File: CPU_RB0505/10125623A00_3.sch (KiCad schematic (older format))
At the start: 45 parts, among them IC10 DS1305E, IC11 OP295, IC12 MAX690ACSA, IC31 M41T94MQ6E, Q3 32,768KHz, Q5 32,768KHz, T14 2N7002, T20 BS170F, T21 2N7002, T3 BSS84

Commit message: Schematic symbols updated with BOM fields
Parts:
- BUZ1: Description (none) -> BUZZER, 12V, 30MA, 85DB; Item Number (none) -> 10023244; Manufacturer (none) -> STAR MICRONICS INC.; Manufacturer_Desc (none) -> MAGNETIC BUZZER; Manufacturer_No (none) -> HMB-12
- C39, C43, C45, C50, C53: Description (none) -> CAPACITOR CERAMIC,10NF,+/-10%,50V,0603; Item Number (none) -> 10022508; Manufacturer (none) -> YAGEO_RMS1; Manufacturer2 (none) -> YAGEO_RMS1; Manufacturer3 (none) -> KEMET_RMS1; Manufacturer4 (none) -> YAGEO_RMS1; Manufacturer_Desc (none) -> CAPACITOR, CERAMIC, MULTILAYER, 50 V, X7R, 0.01 UF, SURFACE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; Manufacturer_Desc2 (none) -> CAPACITOR, CERAMIC, MULTILAYER, 50 V, X7R, 0.01 UF, SURFACE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; Manufacturer_Desc3 (none) -> CERAMIC CHIP CAPACITOR; Manufacturer_Desc4 (none) -> CAPACITOR, CERAMIC, MULTILAYER, 50 V, X7R, 0.01 UF, SURFACE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; Manufacturer_No (none) -> 223858615636; Manufacturer_No2 (none) -> 223858615536; Manufacturer_No3 (none) -> C0603C103K5RACTU; Manufacturer_No4 (none) -> CC0603KRX7R9BB103
- C42, C44, C49, C77, C78: Description (none) -> CAPACITOR,100NF,16V,+/-10%,X7R,0402; Item Number (none) -> 10022607; Manufacturer (none) -> MURATA; Manufacturer2 (none) -> YAGEO_RMS1; Manufacturer3 (none) -> YAGEO_RMS1; Manufacturer4 (none) -> MURATA MANUFACTURING CO., LTD.; Manufacturer_Desc (none) -> CAPACITOR, CERAMIC, MULTILAYER, 16V, X7R, 0.1UF, 0402; Manufacturer_Desc2 (none) -> CAP CER 0.1uF 16V X7R 10% 0402; Manufacturer_Desc3 (none) -> CAPACITOR, CERAMIC, MULTILAYER, 16 V, X7R, 0.1 UF, SURFACE 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; Manufacturer_Desc4 (none) -> MONOLITHIC CERAMIC CAPACITOR; Manufacturer_No (none) -> GRM155R71C104JA88J; Manufacturer_No2 (none) -> CC0402KRX7R7BB104; Manufacturer_No3 (none) -> 223878715649; Manufacturer_No4 (none) -> GRM155R71C104KA88D
- C54: Description (none) -> CAPACITOR CERAMIC,1UF,16V,+/-10%, 0805; Item Number (none) -> 10022967; Manufacturer (none) -> KEMET_RMS1; Manufacturer2 (none) -> KEMET_RMS1; Manufacturer3 (none) -> YAGEO_RMS1; Manufacturer4 (none) -> MURATA_RMS1; Manufacturer_Desc (none) -> CERAMIC CHIP CAPACITOR; Manufacturer_Desc2 (none) -> CERAMIC SURFACE MOUNT; Manufacturer_Desc3 (none) -> CAPACITOR, CERAMIC, MULTILAYER, 16 V, Y5V, 1 UF, SURFACE MO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; Manufacturer_Desc4 (none) -> MONOLITHIC CERAMIC CAPACITOR; Manufacturer_No (none) -> C0805C105Z4VACTU; Manufacturer_No2 (none) -> C0805C105Z4VAC; Manufacturer_No3 (none) -> CC0805ZRY5V7BB105; Manufacturer_No4 (none) -> GRM216B31C105KA87D
- C84: Description (none) -> CAPACITOR CERAMIC, 1NF,50V,+/-10%, 0402; Item Number (none) -> 10022971; Manufacturer (none) -> YAGEO_RMS1; Manufacturer2 (none) -> YAGEO_RMS1; Manufacturer3 (none) -> KEMET_RMS1; Manufacturer4 (none) -> YAGEO_RMS1; Manufacturer_Desc (none) -> CAPACITOR, CERAMIC, MULTILAYER, 50 V, X7R, 0.001 UF, SURFAC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; Manufacturer_Desc2 (none) -> CAPACITOR, CERAMIC, MULTILAYER, 50 V, X7R, 0.001 UF, SURFAC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; Manufacturer_Desc3 (none) -> CAP, CER, 0.001UF, 50V, 10%, X7R, 0402; Manufacturer_Desc4 (none) -> CAPACITOR, CERAMIC, MULTILAYER, 50 V, X7R, 0.001 UF, SURFAC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; Manufacturer_No (none) -> CC0402KRX7R9BB102*; Manufacturer_No2 (none) -> 223858715623; Manufacturer_No3 (none) -> C0402C102K5RACTU; Manufacturer_No4 (none) -> 223858715523
- D12: Description (none) -> DIODE ZENER, 500MW, 12V, SOD-80C; Item Number (none) -> 10020994; Manufacturer (none) -> NXP SEMICONDUCTORS_RMS1; Manufacturer2 (none) -> NXP SEMICONDUCTORS_RMS1; Manufacturer_Desc2 (none) -> VOLTAGE REGULATOR DIODE; Manufacturer_No (none) -> BZV55-C12,115; Manufacturer_No2 (none) -> BZV55-C12
- D14: Description (none) -> DIODE SCHOTTKY DOUBLE,30V, 200MA,SOT23; Item Number (none) -> 10022653; Manufacturer (none) -> NXP SEMICONDUCTORS_RMS1; Manufacturer2 (none) -> NXP SEMICONDUCTORS_RMS1; Manufacturer_Desc2 (none) -> SCHOTTKY BARRIER DOUBLE DIODE; Manufacturer_No (none) -> BAT54C,215; Manufacturer_No2 (none) -> BAT54C
- D15, D16: Description (none) -> DIODE SCHOTTKY, 40V, 1A; Item Number (none) -> 10097253; Manufacturer (none) -> DIODES INC_RMS1; Manufacturer_Desc (none) -> SURFACE MOUNT SCHOTTKY BARRIER RECTIFIER; Manufacturer_No (none) -> 1N5819HW-7-F
- G1: Description (none) -> LITHIUM, 3V, 35MAH; Item Number (none) -> 10022884; Manufacturer (none) -> SONY_RMS1; Manufacturer2 (none) -> MAXELL; Manufacturer3 (none) -> VARTA (917650); Manufacturer_Desc (none) -> COIN CELL BATTERY; Manufacturer_Desc3 (none) -> BATTERY; Manufacturer_No (none) -> CR1220-B1A; Manufacturer_No2 (none) -> CR1220; Manufacturer_No3 (none) -> CR 1220
- IC10: Description (none) -> IC,REALTIMECLOCK, TSSOP; Item Number (none) -> 10022965; Manufacturer (none) -> MAXIM_RMS1; Manufacturer2 (none) -> MAXIM_RMS1; Manufacturer_No (none) -> DS1305E+; Manufacturer_No2 (none) -> DS1305E+T&R
- IC11: Description (none) -> DOUBLE AMPLIFIER RAIL TO RAIL, SO8; Item Number (none) -> 10022969; Manufacturer (none) -> ANALOG DEVICES, INC.; Manufacturer2 (none) -> ANALOG DEVICES, INC.; Manufacturer_Desc (none) -> IC OPAMP GP R-R 85KHZ DUAL 8SOIC; Manufacturer_Desc2 (none) -> IC OPAMP DUAL RAIL-RAIL 8SOIC; Manufacturer_No (none) -> OP295GSZ-REEL7; Manufacturer_No2 (none) -> OP295GSZ
- IC12: Description (none) -> IC,MICROPROCESSOR SUPERVISOR CIRCUIT,SO8; Item Number (none) -> 10022970; Manufacturer (none) -> MAXIM_RMS1; Manufacturer2 (none) -> MAXIM_RMS1; Manufacturer_Desc2 (none) -> MICROPROCESSOR SUPERVISORY CIRCUIT; Manufacturer_No (none) -> MAX690ACSA+T; Manufacturer_No2 (none) -> MAX690ACSA+
- Q5: Description (none) -> CRYSTAL QUARTZ 32.768KHZ; Item Number (none) -> 10023250; Manufacturer (none) -> IQD; Manufacturer_Desc (none) -> CRYSTAL QUARTZ 32.768KHZ; Manufacturer_No (none) -> LFXTAL003000REEL
- R17: Description (none) -> RESISTOR, 15K OHM, 0603, +/-1%; Item Number (none) -> 10023238; Manufacturer (none) -> ASJ; Manufacturer2 (none) -> VISHAY_RMS1; Manufacturer3 (none) -> YAGEO_RMS1; Manufacturer4 (none) -> YAGEO_RMS1; Manufacturer5 (none) -> YAGEO_RMS1; Manufacturer_Desc2 (none) -> THICK FILM RECTANGULAR CHIP RESISTOR; Manufacturer_Desc3 (none) -> RESISTOR, METAL GLAZE/THICK FILM, 0.1 W, 1 %, 100 PPM, 1500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; Manufacturer_Desc4 (none) -> RESISTOR, METAL GLAZE/THICK FILM, 0.1 W, 1 %, 100 PPM, 1500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; Manufacturer_Desc5 (none) -> RESISTOR, METAL GLAZE/THICK FILM, 0.1 W, 1 %, 100 PPM, 1500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; Manufacturer_No (none) -> CR16153FL; Manufacturer_No2 (none) -> CRCW060315K0FKEA; Manufacturer_No3 (none) -> 232270461503L; Manufacturer_No4 (none) -> RC0603FR-0715KL; Manufacturer_No5 (none) -> 232270461503
- R18: Description (none) -> RESISTOR,1.5K OHM,0.063W,+/-1%,0603; Item Number (none) -> 10022700; Manufacturer (none) -> YAGEO_RMS1; Manufacturer2 (none) -> YAGEO_RMS1; Manufacturer3 (none) -> KOA SPEER; Manufacturer4 (none) -> YAGEO_RMS1; Manufacturer_Desc (none) -> RESISTOR, METAL GLAZE/THICK FILM, 0.1 W, 1 %, 100 PPM, 1500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; Manufacturer_Desc2 (none) -> RESISTOR, METAL GLAZE/THICK FILM, 0.1 W, 1 %, 100 PPM, 1500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; Manufacturer_Desc3 (none) -> THICK FILM CHIP RESISTOR; Manufacturer_Desc4 (none) -> RESISTOR, METAL GLAZE/THICK FILM, 0.1 W, 1 %, 100 PPM, 1500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; Manufacturer_No (none) -> 232270461502; Manufacturer_No2 (none) -> 232270461502L; Manufacturer_No3 (none) -> RK73H1JTTD1501F; Manufacturer_No4 (none) -> RC0603FR-071K5L
- R19: Description (none) -> RESISTOR, 75K OHM, 0603, +/-1%; Item Number (none) -> 10023239; Manufacturer (none) -> MULTICOMP (920630); Manufacturer_Desc (none) -> THICK FILM CHIP RESISTOR; Manufacturer_No (none) -> MC 0.063W 0603 1% 75K
- R28, R29, R53, R54: Description (none) -> RESISTOR,10K OHM, 0.063W,+/-5%,0603; Item Number (none) -> 10097266; Manufacturer (none) -> YAGEO_RMS1; Manufacturer2 (none) -> YAGEO_RMS1; Manufacturer3 (none) -> VISHAY_RMS1; Manufacturer4 (none) -> ASJ; Manufacturer5 (none) -> YAGEO_RMS1; Manufacturer_Desc (none) -> RESISTOR, METAL GLAZE/THICK FILM, 0.1 W, 5 %, 100 PPM, 1000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; Manufacturer_Desc2 (none) -> RESISTOR, METAL GLAZE/THICK FILM, 0.1 W, 5 %, 100 PPM, 1000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; Manufacturer_Desc3 (none) -> THICK FILM RECTANGULAR CHIP RESISTOR; Manufacturer_Desc4 (none) -> THICK FILM CHIP RESISTOR; Manufacturer_Desc5 (none) -> RESISTOR, METAL GLAZE/THICK FILM, 0.1 W, 5 %, 100 PPM, 1000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; Manufacturer_No (none) -> 232270260103L; Manufacturer_No2 (none) -> 232270260103; Manufacturer_No3 (none) -> CRCW060310K0JNEA; Manufacturer_No4 (none) -> CR16-103JL; Manufacturer_No5 (none) -> RC0603JR-0710KL
- R52: Description (none) -> RESISTOR 10 OHM, 0.125W, +/-5%,0805; Item Number (none) -> 10023242; Manufacturer (none) -> YAGEO_RMS1; Manufacturer2 (none) -> KOA SPEER; Manufacturer3 (none) -> YAGEO_RMS1; Manufacturer4 (none) -> YAGEO_RMS1; Manufacturer_Desc (none) -> RESISTOR, METAL GLAZE/THICK FILM, 0.125 W, 5 %, 200 PPM, 10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; Manufacturer_Desc2 (none) -> THICK FILM CHIP RESISTOR; Manufacturer_Desc3 (none) -> RESISTOR, METAL GLAZE/THICK FILM, 0.125 W, 5 %, 200 PPM, 10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; Manufacturer_Desc4 (none) -> RESISTOR, METAL GLAZE/THICK FILM, 0.125 W, 5 %, 200 PPM, 10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; Manufacturer_No (none) -> RC0805JR-0710RL; Manufacturer_No2 (none) -> RK73B2ATTD100J; Manufacturer_No3 (none) -> 232273061109L; Manufacturer_No4 (none) -> 232273061109
- R55, R56, R59, R65, R8, R9: Description (none) -> RESISTOR,100 K OHM, 0.063W +/-5%; Item Number (none) -> 10022732; Manufacturer (none) -> YAGEO_RMS1; Manufacturer2 (none) -> YAGEO_RMS1; Manufacturer3 (none) -> YAGEO_RMS1; Manufacturer4 (none) -> PANASONIC_RMS1; Manufacturer_Desc (none) -> RESISTOR, METAL GLAZE/THICK FILM, 0.1 W, 5 %, 100 PPM, 1000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; Manufacturer_Desc2 (none) -> RESISTOR, METAL GLAZE/THICK FILM, 0.1 W, 5 %, 100 PPM, 1000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; Manufacturer_Desc3 (none) -> RESISTOR, METAL GLAZE/THICK FILM, 0.1 W, 5 %, 100 PPM, 1000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; Manufacturer_Desc4 (none) -> THICK FILM CHIP RESISTOR; Manufacturer_No (none) -> 232270260104L; Manufacturer_No2 (none) -> 232270260104; Manufacturer_No3 (none) -> RC0603JR-07100KL; Manufacturer_No4 (none) -> ERJ3GEYJ104V
- R57: Description (none) -> RESISTOR,1.37K OHM,0.063W,+/-0.1%,0603; Item Number (none) -> 10097270; Manufacturer (none) -> SUSUMU CO.; Manufacturer2 (none) -> TYCO ELECTRONICS; Manufacturer3 (none) -> TYCO ELECTRONICS; Manufacturer4 (none) -> VISHAY_RMS1; Manufacturer5 (none) -> WELWYN; Manufacturer_Desc2 (none) -> THIN FILM PRECISION CHIP RESISTOR; Manufacturer_Desc3 (none) -> THIN FILM PRECISION CHIP RESISTOR; Manufacturer_Desc4 (none) -> PRECISION CHIP RESISTOR; Manufacturer_Desc5 (none) -> PRECISION SURFACE MOUNT RESISTOR; Manufacturer_No (none) -> RG1608P-1371-B-T5; Manufacturer_No2 (none) -> 3-1879219-4; Manufacturer_No3 (none) -> CPF0603B-1K37E; Manufacturer_No4 (none) -> TNPW06031K37BEEA; Manufacturer_No5 (none) -> PCF0603R-1K37BI
- R58: Description (none) -> RESISTOR, 100K OHM, 0.063W,+/-0.1%,0603; Item Number (none) -> 10097271; Manufacturer (none) -> SUSUMU CO.; Manufacturer2 (none) -> WELWYN; Manufacturer3 (none) -> YAGEO_RMS1; Manufacturer_Desc (none) -> RES SMD 100K OHM 0.1% 1/10W 0603; Manufacturer_Desc2 (none) -> LOW VALUE FLAT CHIP RESISTOR; Manufacturer_Desc3 (none) -> RESISTOR, THIN FILM, 0.1 W, 0.1 %, 25 PPM, 100000 OHM, SURF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; Manufacturer_No (none) -> RG1608P-104-B-T5; Manufacturer_No2 (none) -> PCF0603R-100KBI; Manufacturer_No3 (none) -> RT0603BRD07100KL
- T14, T21: Description (none) -> TRANSISTOR MOSFET N CHANNEL 60V, 0.18A; Item Number (none) -> 10097274; Manufacturer (none) -> ON SEMICONDUCTOR_RMS1; Manufacturer2 (none) -> NXP SEMICONDUCTORS_RMS1; Manufacturer3 (none) -> NXP SEMICONDUCTORS_RMS1; Manufacturer_Desc (none) -> SMALL SIGNAL MOSFET; Manufacturer_Desc3 (none) -> N-CHANNEL TRENCHMOS FET; Manufacturer_No (none) -> 2N7002LT1G; Manufacturer_No2 (none) -> 2N7002,215; Manufacturer_No3 (none) -> 2N7002
- T20: Description (none) -> TRANSISTOR, MOSFET, N-CHANNEL, 60V, 0.5A.SOT23; Item Number (none) -> 10022956; Manufacturer (none) -> FAIRCHILD SEMICONDUCTOR_RMS1; Manufacturer2 (none) -> DIODES INC_RMS1; Manufacturer_Desc (none) -> MOSFET N-CH 60V 500MA SOT-23; Manufacturer_Desc2 (none) -> N-CHANNEL MOSFET; Manufacturer_No (none) -> MMBF170; Manufacturer_No2 (none) -> MMBF170-7-F
- T3: Description (none) -> TRANSISTOR, P CHANNEL, 50V, 0.13A, 5 OHM, SOT23; Item Number (none) -> 10022157; Manufacturer (none) -> NXP SEMICONDUCTORS_RMS1; Manufacturer2 (none) -> ON SEMICONDUCTOR_RMS1; Manufacturer3 (none) -> NXP SEMICONDUCTORS_RMS1; Manufacturer_Desc (none) -> MOSFET P CHANNEL; Manufacturer_Desc2 (none) -> POWER MOSFET; Manufacturer_No (none) -> BSS84; Manufacturer_No2 (none) -> BSS84LT1G; Manufacturer_No3 (none) -> BSS84,215
- V2: Description (none) -> 3 WAY, PROPORTIONAL VALVE; Item Number (none) -> 10025112; Manufacturer (none) -> FAS; Manufacturer_Desc (none) -> 3 WAY PROPORTIONAL VALVE; Manufacturer_No (none) -> S142.0048A

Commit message: back anotate from cmp file
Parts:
- BUZ1: footprint 10125623A00:F_HMB -> AllModules:HMB12_1
- C39, C43, C45, C50, C53: footprint 10125623A00:C0805 -> AllModules:C0603_1
- C42, C44, C49, C77, C78, C84: footprint 10125623A00:C0805 -> AllModules:C0402_1
- C54: footprint 10125623A00:C0805 -> AllModules:C0805_1
- D12: footprint 10125623A00:SOT23DIO -> AllModules:SOD80_1
- D14: footprint 10125623A00:SOT23_DI -> AllModules:SOT23-1G_1
- D15, D16: footprint 10125623A00:SOD87 -> AllModules:SOD87_1
- G1: footprint 10125623A00:KEY_3000 -> AllModules:CR1220-3000_1
- IC10: footprint 10125623A00:TSSOP20 -> AllModules:TSSOP20_SANS-MIRE_1
- IC11: footprint 10125623A00:SO8 -> AllModules:MX.A8_COMPOSANT_1
- IC12: footprint 10125623A00:SO08 -> AllModules:MX.A8_COMPOSANT_1
- IC31: footprint 10125623A00:SO16 -> AllModules:MX.A16_COMPOSANT_1
- Q3, Q5: footprint 10125623A00:86SMX -> AllModules:85SMX_1
- R17, R18, R19, R28, R29, R53, R54, R55, R56, R57, R58, R59, R65, R8, R9: footprint 10125623A00:R0805 -> AllModules:R0603_1
- R52: footprint 10125623A00:R0805 -> AllModules:R0805_1
- T14, T20, T21: footprint 10125623A00:DPAK -> AllModules:SOT23-GSD_1
- T3: footprint 10125623A00:SOT23MOS -> AllModules:SOT23-GSD_1
- V2: footprint 10125623A00:FAS-PPS-1P-3NIP-INJ -> AllModules:S142.0011-SANS-FIX_1

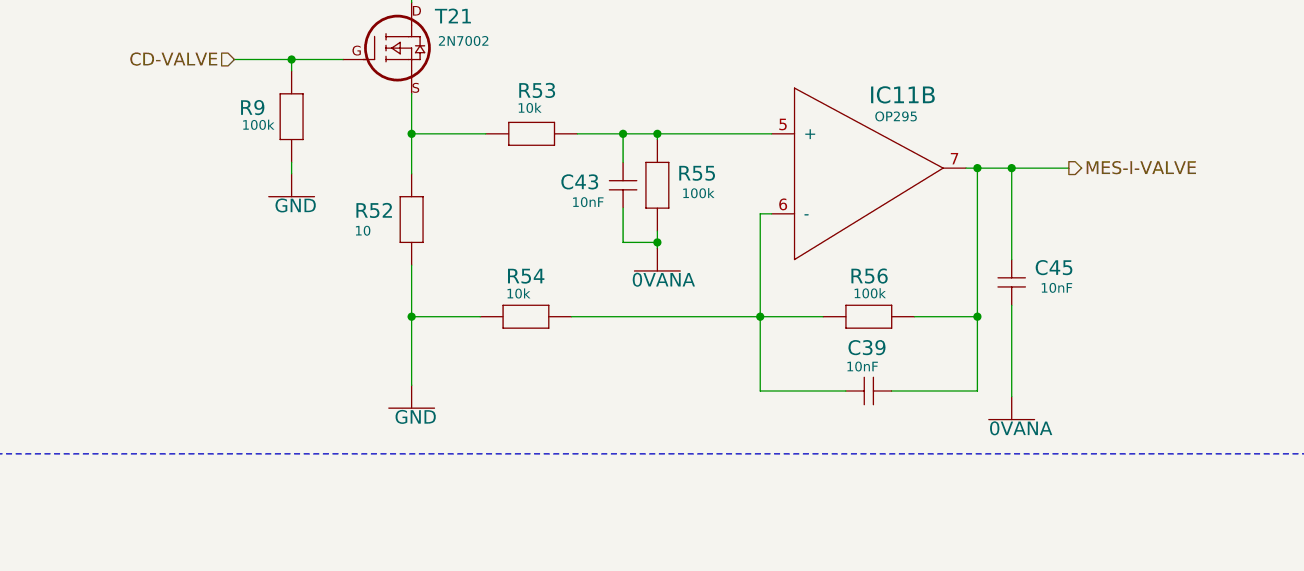
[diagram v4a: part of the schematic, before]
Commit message: fix erc errors, change many pin electrical types
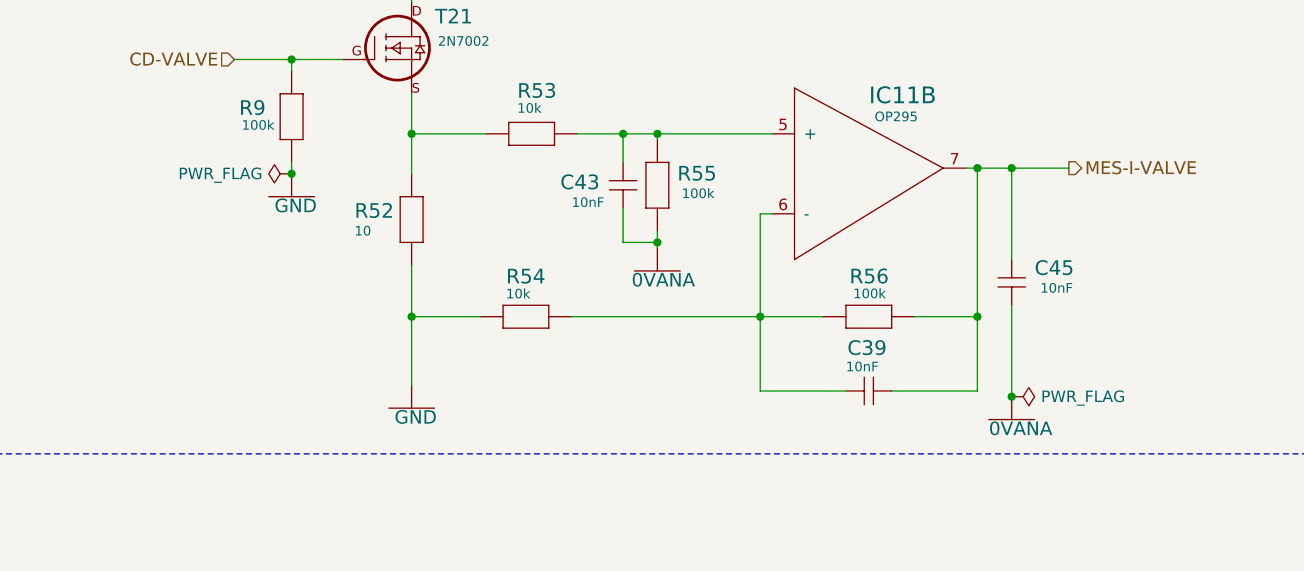
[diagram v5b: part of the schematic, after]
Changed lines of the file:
@@
-$EndComp
-$Comp
-L cpu-board:LM358 IC11
-U 3 1 D9B46218
-P 7325 2700
-AR Path="/D9B46218" Ref="IC11"  Part="3"
-AR Path="/5E924756/D9B46218" Ref="IC11"  Part="3"
-F 0 "IC11" H 7525 2950 73  0001 L BNN
-F 1 "OP295" H 7675 2850 73  0001 L BNN
-F 2 "AllModules:MX.A8_COMPOSANT_1" H 7325 2700 50  0001 C CNN
-F 3 "" H 7325 2700 50  0001 C CNN
-F 4 "DOUBLE AMPLIFIER RAIL TO RAIL, SO8" H 7325 2700 50  0001 C CNN "Description"
-F 5 "10022969" H 7325 2700 50  0001 C CNN "Item Number"
-F 6 "ANALOG DEVICES, INC." H 7325 2700 50  0001 C CNN "Manufacturer"
-F 7 "OP295GSZ-REEL7" H 7325 2700 50  0001 C CNN "Manufacturer_No"
-F 8 "IC OPAMP GP R-R 85KHZ DUAL 8SOIC" H 7325 2700 50  0001 C CNN "Manufacturer_Desc"
-F 9 "ANALOG DEVICES, INC." H 7325 2700 50  0001 C CNN "Manufacturer2"
-F 10 "OP295GSZ" H 7325 2700 50  0001 C CNN "Manufacturer_No2"
-F 11 "IC OPAMP DUAL RAIL-RAIL 8SOIC" H 7325 2700 50  0001 C CNN "Manufacturer_Desc2"
-	3    7325 2700
-	1    0    0    -1
 $EndComp
 $Comp
@@
 NoConn ~ 3225 2850
 NoConn ~ 2125 3350
-$Comp
-L cpu-board:LM358 IC11
-U 1 1 D9B46210
-P 7375 2700
-AR Path="/D9B46210" Ref="IC11"  Part="1"
-AR Path="/5E924756/D9B46210" Ref="IC11"  Part="1"
-F 0 "IC11" H 7425 2950 64  0000 L BNN
-F 1 "OP295" H 7450 2863 42  0000 L BNN
-F 2 "AllModules:MX.A8_COMPOSANT_1" H 7375 2700 50  0001 C CNN
-F 3 "" H 7375 2700 50  0001 C CNN
-F 4 "DOUBLE AMPLIFIER RAIL TO RAIL, SO8" H 7325 2700 50  0001 C CNN "Description"
-F 5 "10022969" H 7325 2700 50  0001 C CNN "Item Number"
-F 6 "ANALOG DEVICES, INC." H 7325 2700 50  0001 C CNN "Manufacturer"
-F 7 "OP295GSZ-REEL7" H 7325 2700 50  0001 C CNN "Manufacturer_No"
-F 8 "IC OPAMP GP R-R 85KHZ DUAL 8SOIC" H 7325 2700 50  0001 C CNN "Manufacturer_Desc"
-F 9 "ANALOG DEVICES, INC." H 7325 2700 50  0001 C CNN "Manufacturer2"
-F 10 "OP295GSZ" H 7325 2700 50  0001 C CNN "Manufacturer_No2"
-F 11 "IC OPAMP DUAL RAIL-RAIL 8SOIC" H 7325 2700 50  0001 C CNN "Manufacturer_Desc2"
-	1    7375 2700
-	1    0    0    -1
-$EndComp
 Wire Wire Line
 	3850 3025 3850 3100
@@
 	3225 4925 3825 4925
 NoConn ~ 3525 5075
+$Comp
+L power:PWR_FLAG #FLG0104
+U 1 1 5ED7B35B
+P 11375 6300
+F 0 "#FLG0104" H 11375 6375 50  0001 C CNN
+F 1 "PWR_FLAG" V 11375 6427 50  0000 L CNN
+F 2 "" H 11375 6300 50  0001 C CNN
+F 3 "~" H 11375 6300 50  0001 C CNN
+	1    11375 6300
+	0    -1   -1   0
+$EndComp
+Connection ~ 11375 6300
+$Comp
+L power:PWR_FLAG #FLG0105
+U 1 1 5ED7BF1F
+P 14525 7275
+F 0 "#FLG0105" H 14525 7350 50  0001 C CNN
+F 1 "PWR_FLAG" V 14525 7403 50  0000 L CNN
+F 2 "" H 14525 7275 50  0001 C CNN
+F 3 "~" H 14525 7275 50  0001 C CNN
+	1    14525 7275
+	0    1    1    0
+$EndComp
+Connection ~ 14525 7275
+$Comp
+L cpu-board:LM358 IC11
+U 1 1 D9B46210
+P 7375 2700
+AR Path="/D9B46210" Ref="IC11"  Part="1"
+AR Path="/5E924756/D9B46210" Ref="IC11"  Part="1"
+F 0 "IC11" H 7425 2950 64  0000 L BNN
+F 1 "OP295" H 7450 2863 42  0000 L BNN
+F 2 "AllModules:MX.A8_COMPOSANT_1" H 7375 2700 50  0001 C CNN
+F 3 "" H 7375 2700 50  0001 C CNN
+F 4 "DOUBLE AMPLIFIER RAIL TO RAIL, SO8" H 7325 2700 50  0001 C CNN "Description"
+F 5 "10022969" H 7325 2700 50  0001 C CNN "Item Number"
+F 6 "ANALOG DEVICES, INC." H 7325 2700 50  0001 C CNN "Manufacturer"
+F 7 "OP295GSZ-REEL7" H 7325 2700 50  0001 C CNN "Manufacturer_No"
+F 8 "IC OPAMP GP R-R 85KHZ DUAL 8SOIC" H 7325 2700 50  0001 C CNN "Manufacturer_Desc"
+F 9 "ANALOG DEVICES, INC." H 7325 2700 50  0001 C CNN "Manufacturer2"
+F 10 "OP295GSZ" H 7325 2700 50  0001 C CNN "Manufacturer_No2"
+F 11 "IC OPAMP DUAL RAIL-RAIL 8SOIC" H 7325 2700 50  0001 C CNN "Manufacturer_Desc2"
+	1    7375 2700
+	1    0    0    -1
+$EndComp
+$Comp
+L cpu-board:LM358 IC11
+U 3 1 D9B46218
+P 7325 2700
+AR Path="/D9B46218" Ref="IC11"  Part="3"
+AR Path="/5E924756/D9B46218" Ref="IC11"  Part="3"
+F 0 "IC11" H 7525 2950 73  0001 L BNN
+F 1 "OP295" H 7675 2850 73  0001 L BNN
+F 2 "AllModules:MX.A8_COMPOSANT_1" H 7325 2700 50  0001 C CNN
+F 3 "" H 7325 2700 50  0001 C CNN
+F 4 "DOUBLE AMPLIFIER RAIL TO RAIL, SO8" H 7325 2700 50  0001 C CNN "Description"
+F 5 "10022969" H 7325 2700 50  0001 C CNN "Item Number"
+F 6 "ANALOG DEVICES, INC." H 7325 2700 50  0001 C CNN "Manufacturer"
+F 7 "OP295GSZ-REEL7" H 7325 2700 50  0001 C CNN "Manufacturer_No"
+F 8 "IC OPAMP GP R-R 85KHZ DUAL 8SOIC" H 7325 2700 50  0001 C CNN "Manufacturer_Desc"
+F 9 "ANALOG DEVICES, INC." H 7325 2700 50  0001 C CNN "Manufacturer2"
+F 10 "OP295GSZ" H 7325 2700 50  0001 C CNN "Manufacturer_No2"
+F 11 "IC OPAMP DUAL RAIL-RAIL 8SOIC" H 7325 2700 50  0001 C CNN "Manufacturer_Desc2"
+	3    7325 2700
+	1    0    0    -1
+$EndComp
 $EndSCHEMATC

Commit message: CPU schematic updated to Kicad resistor and cap symbols
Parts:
- C39, C42, C43, C44, C45, C49, C50, C53, C54, C77, C78, C84: symbol cpu-board:C0805 -> Flipped_Devices:C_Small
- R17, R18, R19, R28, R29, R52, R53, R54, R55, R56, R57, R58, R59, R65, R8, R9: symbol cpu-board:R0805 -> Flipped_Devices:R
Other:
- moved on the sheet: BUZ1, C42, C43, C44, C45, C49, C50, C53, C54, C77, C84, D12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

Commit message: CPU board diode and transistor symbols changed to Kicad symbols
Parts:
- D12: symbol cpu-board:BZX84CXX -> Flipped_Devices:D_Zener_A1K3
- D15, D16: symbol cpu-board:PRLL5819 -> Flipped_Devices:D_Schottky
- IC11: symbol cpu-board:LM358 -> Device:Opamp_Dual_Generic
- Q3, Q5: symbol cpu-board:86SMX -> Flipped_Devices:Crystal_Small_Pin1Pin4
- T14, T20, T21: symbol cpu-board:MTD3055 -> Flipped_Devices:Q_NMOS_GSD
- T3: symbol cpu-board:IRLML5103 -> Flipped_Devices:Q_PMOS_GSD

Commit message: ran renameSchSyms.py
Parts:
- BUZ1: symbol cpu-board:F_HMB -> Buzzer:F_HMB
- C39, C43, C45, C50, C53: symbol Flipped_Devices:C_Small -> Capacitor:C0603_10nF_50V_10%
- C42, C44, C49, C77, C78: symbol Flipped_Devices:C_Small -> Capacitor:C0402_100nF_16V_10%
- C54: symbol Flipped_Devices:C_Small -> Capacitor:C0805_1uF_16V_10%
- C84: symbol Flipped_Devices:C_Small -> Capacitor:C0402_1nF_50V_10%
- D12: symbol Flipped_Devices:D_Zener_A1K3 -> Diode:D_Zener_A1K3_10020994
- D14: symbol cpu-board:BAT54C -> Diode:BAT54C
- D15, D16: symbol Flipped_Devices:D_Schottky -> Diode:D_Schottky
- G1: symbol cpu-board:KEY_3000 -> Battery:KEY_3000
- IC10: symbol cpu-board:DS1305E -> IC:DS1305E
- IC11: symbol Device:Opamp_Dual_Generic -> IC:Opamp_Dual_Generic
- IC12: symbol cpu-board:MAX690ACSA -> IC:MAX690ACSA
- Q5: symbol Flipped_Devices:Crystal_Small_Pin1Pin4 -> Crystal:Crystal_Small_Pin1Pin4
- R17: symbol Flipped_Devices:R -> Resistor:R0603_15k_1%
- R18: symbol Flipped_Devices:R -> Resistor:R0603_1k5_1%
- R19: symbol Flipped_Devices:R -> Resistor:R0603_75k_1%
- R28, R29, R53, R54: symbol Flipped_Devices:R -> Resistor:R0603_10k_5%
- R52: symbol Flipped_Devices:R -> Resistor:R0805_10R_5%
- R55, R56, R59, R65, R8, R9: symbol Flipped_Devices:R -> Resistor:R_100k_5%
- R57: symbol Flipped_Devices:R -> Resistor:R0603_1k37_0.1%
- R58: symbol Flipped_Devices:R -> Resistor:R0603_100k_0.1%_10097271
- T14, T21: symbol Flipped_Devices:Q_NMOS_GSD -> Transistor:Q_NMOS_GSD_10097274
- T20: symbol Flipped_Devices:Q_NMOS_GSD -> Transistor:Q_NMOS_GSD_10022956
- T3: symbol Flipped_Devices:Q_PMOS_GSD -> Transistor:Q_PMOS_GSD_10022157
- V2: symbol cpu-board:FAS-PPS-1P-3NIP-INJ -> Valve:FAS-PPS-1P-3NIP-INJ
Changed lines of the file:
@@
 $EndComp
 $Comp
-L Flipped_Devices:C_Small C42
+L Capacitor:C0402_100nF_16V_10% C42
 U 1 1 E64E96FA
 P 3050 4950
@@
 $EndComp
 $Comp
-L cpu-board:DS1305E IC10
+L IC:DS1305E IC10
 U 1 1 E884BF5E
 P 3250 6250
@@
 $EndComp
 $Comp
-L cpu-board:KEY_3000 G1
+L Battery:KEY_3000 G1
 U 1 1 7E939E76
 P 4550 6750
@@
 $EndComp
 $Comp
-L Flipped_Devices:R R8
+L Resistor:R_100k_5% R8
 U 1 1 C507FD3A
 P 13200 3350
@@
 $EndComp
 $Comp
-L Flipped_Devices:D_Schottky D15
+L Diode:D_Schottky D15
 U 1 1 557FCCAF
 P 13550 2600
@@
 $EndComp
 $Comp
-L Flipped_Devices:R R9
+L Resistor:R_100k_5% R9
 U 1 1 D76F26ED
 P 11350 6050
@@
 $EndComp
 $Comp
-L Flipped_Devices:D_Schottky D16
+L Diode:D_Schottky D16
 U 1 1 16F46E82
 P 11900 5000
@@
 $EndComp
 $Comp
-L cpu-board:FAS-PPS-1P-3NIP-INJ V2
+L Valve:FAS-PPS-1P-3NIP-INJ V2
 U 1 1 F1FC2759
 P 13550 5250
@@
 $EndComp
 $Comp
-L Flipped_Devices:R R53
+L Resistor:R0603_10k_5% R53
 U 1 1 CFBE9597
 P 12450 6100
@@
 $EndComp
 $Comp
-L Flipped_Devices:R R54
+L Resistor:R0603_10k_5% R54
 U 1 1 E78706DF
 P 12400 6950
@@
 $EndComp
 $Comp
-L Flipped_Devices:R R55
+L Resistor:R_100k_5% R55
 U 1 1 19D405B0
 P 13000 6350
@@
 $EndComp
 $Comp
-L Flipped_Devices:R R56
+L Resistor:R_100k_5% R56
 U 1 1 D165D9D0
 P 13900 6950
@@
 $EndComp
 $Comp
-L Flipped_Devices:C_Small C39
+L Capacitor:C0603_10nF_50V_10% C39
 U 1 1 849D34A1
 P 13900 7250
@@
 $EndComp
 $Comp
-L Flipped_Devices:C_Small C43
+L Capacitor:C0603_10nF_50V_10% C43
 U 1 1 A25B9E4F
 P 12850 6350
@@
 $EndComp
 $Comp
-L Flipped_Devices:C_Small C45
+L Capacitor:C0603_10nF_50V_10% C45
 U 1 1 72A1248A
 P 14550 6750
@@
 $EndComp
 $Comp
-L Flipped_Devices:R R52
+L Resistor:R0805_10R_5% R52
 U 1 1 9AA44C7C
 P 11900 6500
@@
 $EndComp
 $Comp
-L Flipped_Devices:R R57
+L Resistor:R0603_1k37_0.1% R57
 U 1 1 E37BEEA0
 P 6650 3950
@@
 $EndComp
 $Comp
-L Flipped_Devices:R R58
+L Resistor:R0603_100k_0.1%_10097271 R58
 U 1 1 699A423E
 P 7350 3750
@@
 $EndComp
 $Comp
-L Flipped_Devices:C_Small C53
+L Capacitor:C0603_10nF_50V_10% C53
 U 1 1 EE013C0B
 P 6400 3250
@@
 $EndComp
 $Comp
-L Flipped_Devices:C_Small C54
+L Capacitor:C0805_1uF_16V_10% C54
 U 1 1 B2D23927
 P 7350 3950
@@
 $EndComp
 $Comp
-L Flipped_Devices:C_Small C78
+L Capacitor:C0402_100nF_16V_10% C78
 U 1 1 7765160B
 P 7600 2200
@@
 $EndComp
 $Comp
-L Flipped_Devices:C_Small C84
+L Capacitor:C0402_1nF_50V_10% C84
 U 1 1 86B4EA67
 P 8050 3000
@@
 $EndComp
 $Comp
-L Flipped_Devices:R R59
+L Resistor:R_100k_5% R59
 U 1 1 C270A6BB
 P 6200 3250
@@
 $EndComp
 $Comp
-L Flipped_Devices:R R65
+L Resistor:R_100k_5% R65
 U 1 1 3D749CE4
 P 10550 3500
@@
 $EndComp
 $Comp
-L Flipped_Devices:C_Small C44
+L Capacitor:C0402_100nF_16V_10% C44
 U 1 1 43269358
 P 2650 2250
@@
 $EndComp
 $Comp
-L Flipped_Devices:R R17
+L Resistor:R0603_15k_1% R17
 U 1 1 73F99271
 P 1700 3300
@@
 $EndComp
 $Comp
-L Flipped_Devices:R R18
+L Resistor:R0603_1k5_1% R18
 U 1 1 2BB405CC
 P 1700 3750
@@
 $EndComp
 $Comp
-L Flipped_Devices:R R19
+L Resistor:R0603_75k_1% R19
 U 1 1 9DB3FBAD
 P 2600 3750
@@
 $EndComp
 $Comp
-L Flipped_Devices:R R28
+L Resistor:R0603_10k_5% R28
 U 1 1 29F9BCC2
 P 3350 2450
@@
 $EndComp
 $Comp
-L Flipped_Devices:C_Small C49
+L Capacitor:C0402_100nF_16V_10% C49
 U 1 1 36DDF578
 P 1900 3800
@@
 $EndComp
 $Comp
-L Flipped_Devices:C_Small C50
+L Capacitor:C0603_10nF_50V_10% C50
 U 1 1 38BC030E
 P 3500 3800
@@
 $EndComp
 $Comp
-L Flipped_Devices:Q_PMOS_GSD T3
+L Transistor:Q_PMOS_GSD_10022157 T3
 U 1 1 22208D74
 P 3750 3300
@@
 $EndComp
 $Comp
-L Flipped_Devices:R R29
+L Resistor:R0603_10k_5% R29
 U 1 1 437CF36C
 P 3850 3850
@@
 	8000 6950 8100 6950
 $Comp
-L Device:Opamp_Dual_Generic IC11
+L IC:Opamp_Dual_Generic IC11
 U 2 1 D9B4621C
 P 13850 6200
@@
 	4550 6950 4550 7200
 $Comp
-L cpu-board:MAX690ACSA IC12
+L IC:MAX690ACSA IC12
 U 1 1 EEDDF45D
 P 2600 3000
@@
 $EndComp
 $Comp
-L cpu-board:BAT54C D14
+L Diode:BAT54C D14
 U 1 1 DDBEAB72
 P 10050 3300
@@
 Connection ~ 14550 7250
 $Comp
-L Device:Opamp_Dual_Generic IC11
+L IC:Opamp_Dual_Generic IC11
 U 1 1 D9B46210
 P 7350 2650
@@
 $EndComp
 $Comp
-L Device:Opamp_Dual_Generic IC11
+L IC:Opamp_Dual_Generic IC11
 U 3 1 D9B46218
 P 7400 2650
@@
 	7200 4950 7000 4950
 $Comp
-L Flipped_Devices:C_Small C77
+L Capacitor:C0402_100nF_16V_10% C77
 U 1 1 28576E5F
 P 7300 4950
@@
 Connection ~ 11050 3700
 $Comp
-L cpu-board:F_HMB BUZ1
+L Buzzer:F_HMB BUZ1
 U 1 1 A198C796
 P 11150 2750
@@
 	4100 5950 4350 5950
 $Comp
-L Flipped_Devices:Crystal_Small_Pin1Pin4 Q5
+L Crystal:Crystal_Small_Pin1Pin4 Q5
 U 1 1 4396189E
 P 4350 5800
@@
 	14150 6200 14400 6200
 $Comp
-L Flipped_Devices:Q_NMOS_GSD T14
+L Transistor:Q_NMOS_GSD_10097274 T14
 U 1 1 B63BD651
 P 10950 3300
@@
 $EndComp
 $Comp
-L Flipped_Devices:Q_NMOS_GSD T20
+L Transistor:Q_NMOS_GSD_10022956 T20
 U 1 1 71F1869B
 P 13450 3050
@@
 $EndComp
 $Comp
-L Flipped_Devices:Q_NMOS_GSD T21
+L Transistor:Q_NMOS_GSD_10097274 T21
 U 1 1 2CDC58F9
 P 11800 5800
@@
 	11900 5150 11900 5300
 $Comp
-L Flipped_Devices:D_Zener_A1K3 D12
+L Diode:D_Zener_A1K3_10020994 D12
 U 1 1 6864D7E9
 P 11050 2400
